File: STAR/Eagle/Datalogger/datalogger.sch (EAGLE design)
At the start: 9 parts, among them U1 MT25QL01GBBB8ESF-0AAT

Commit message: datalogger v. 2
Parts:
- removed C1: 100nF, resistor:C-USC0603
- removed CONNECTOR: J30J-31J30, CM_J30J:J30J-31J30
- removed R1: 4.7k, resistor:R-US_R0603
- removed U1: MT25QL01GBBB8ESF-0AAT, NR_IC:MT25QL01GBBB8ESF-0AAT
- added J1: J30J-25, CM_J30J:J30J-25
- added U$5: W25N01GV, NR_IC:W25N01GV
- R2: value (none) -> 1M
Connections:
- removed net N$1: R1.2, U1.!RESET!, U1.DQ3/!HOLD!
- removed net N$10: CONNECTOR.11
- removed net N$12: CONNECTOR.13
- removed net N$2: CONNECTOR.3
- removed net N$3: CONNECTOR.4
- removed net N$4: CONNECTOR.5
- removed net N$5: CONNECTOR.6
- removed net N$6: CONNECTOR.7
- removed net N$7: CONNECTOR.8
- removed net N$8: CONNECTOR.9
- removed net N$9: CONNECTOR.10
- removed net PB23: CONNECTOR.2, U1.!S!
- new net B: J1.18
- new net F: J1.9
- new net H: J1.19
- new net J: J1.6
- new net R: J1.14
- new net S: J1.7
- new net V: J1.8
- new net Y: J1.10
- net +3V3: now also J1.12, U$5.VCC; no longer C1.1, CONNECTOR.21, R1.1, U1.VCC
- net +5V: now also J1.15; no longer CONNECTOR.29
- net DATA1_N: now also J1.2; no longer CONNECTOR.22
- net DATA1_P: now also J1.4; no longer CONNECTOR.23
- net DATA2_N: now also J1.23; no longer CONNECTOR.25
- net DATA2_P: now also J1.22; no longer CONNECTOR.24
- net DATA3_N: now also J1.16; no longer CONNECTOR.30
- net DATA3_P: now also J1.17; no longer CONNECTOR.31
- net DATA4_N: now also J1.21; no longer CONNECTOR.16
- net DATA4_P: now also J1.20; no longer CONNECTOR.15
- net GND: now also J1.13, U$5.CS, U$5.GND, U$5.PAD; no longer C1.2, CONNECTOR.12, CONNECTOR.14, CONNECTOR.26, U1.VSS
- net MISO_FLASH: now also J1.1, U$5.MISO; no longer CONNECTOR.1, U1.DQ1
- net MISO_STAR: now also J1.25; no longer CONNECTOR.27
- net MOSI_FLASH: now also J1.3, U$5.MOSI; no longer CONNECTOR.18, U1.DQ0
- net MOSI_STAR: no longer CONNECTOR.19
- net SCK_FLASH: now also J1.5, U$5.CLK; no longer CONNECTOR.17, U1.C
- net SCK_STAR: now also J1.11; no longer CONNECTOR.20
- net SD_STAR: now also J1.24; no longer CONNECTOR.28

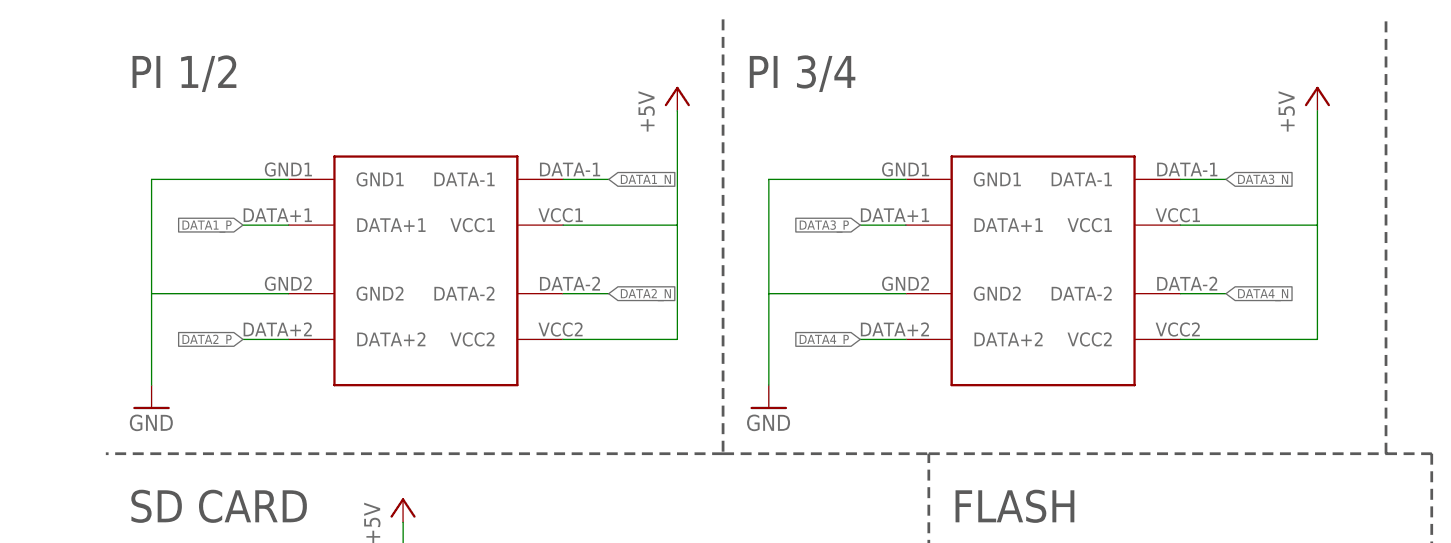
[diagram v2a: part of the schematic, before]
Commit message: fixed datalogger USB port
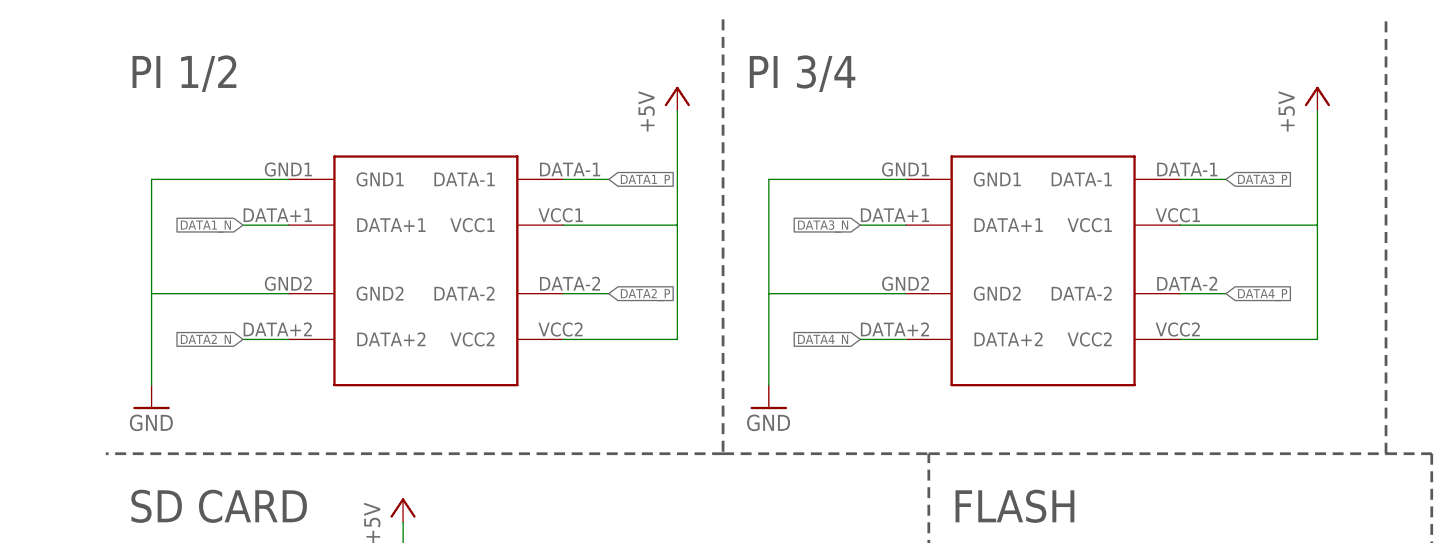
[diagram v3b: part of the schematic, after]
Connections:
- net DATA1_N: now also U$2.DATA+1; no longer U$2.DATA-1
- net DATA1_P: now also U$2.DATA-1; no longer U$2.DATA+1
- net DATA2_N: now also U$2.DATA+2; no longer U$2.DATA-2
- net DATA2_P: now also U$2.DATA-2; no longer U$2.DATA+2
- net DATA3_N: now also U$3.DATA+1; no longer U$3.DATA-1
- net DATA3_P: now also U$3.DATA-1; no longer U$3.DATA+1
- net DATA4_N: now also U$3.DATA+2; no longer U$3.DATA-2
- net DATA4_P: now also U$3.DATA-2; no longer U$3.DATA+2
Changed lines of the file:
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@@
 <net name="DATA1_P" class="0">
+<segment>
+<pinref part="J1" gate="G$1" pin="4"/>
+<wire x1="35.56" y1="106.68" x2="33.02" y2="106.68" width="0.1524" layer="91"/>
+<label x="33.02" y="106.68" size="1.016" layer="95" rot="R180" xref="yes"/>
+</segment>
+<segment>
+<pinref part="U$2" gate="G$1" pin="DATA-1"/>
+<wire x1="60.96" y1="254" x2="66.04" y2="254" width="0.1524" layer="91"/>
+<label x="66.04" y="254" size="1.016" layer="95" xref="yes"/>
+</segment>
+</net>
+<net name="DATA1_N" class="0">
+<segment>
+<pinref part="J1" gate="G$1" pin="2"/>
+<wire x1="35.56" y1="116.84" x2="33.02" y2="116.84" width="0.1524" layer="91"/>
+<label x="33.02" y="116.84" size="1.016" layer="95" rot="R180" xref="yes"/>
+</segment>
 <segment>
 <pinref part="U$2" gate="G$1" pin="DATA+1"/>
@@
 <label x="25.4" y="248.92" size="1.016" layer="95" rot="R180" xref="yes"/>
 </segment>
+</net>
+<net name="DATA2_P" class="0">
 <segment>
-<pinref part="J1" gate="G$1" pin="4"/>
-<wire x1="35.56" y1="106.68" x2="33.02" y2="106.68" width="0.1524" layer="91"/>
-<label x="33.02" y="106.68" size="1.016" layer="95" rot="R180" xref="yes"/>
+<pinref part="J1" gate="G$1" pin="22"/>
+<wire x1="45.72" y1="78.74" x2="48.26" y2="78.74" width="0.1524" layer="91"/>
+<label x="48.26" y="78.74" size="1.016" layer="95" xref="yes"/>
+</segment>
+<segment>
+<pinref part="U$2" gate="G$1" pin="DATA-2"/>
+<wire x1="60.96" y1="241.3" x2="66.04" y2="241.3" width="0.1524" layer="91"/>
+<label x="66.04" y="241.3" size="1.016" layer="95" xref="yes"/>
 </segment>
 </net>
-<net name="DATA1_N" class="0">
+<net name="DATA2_N" class="0">
 <segment>
-<pinref part="U$2" gate="G$1" pin="DATA-1"/>
-<wire x1="60.96" y1="254" x2="66.04" y2="254" width="0.1524" layer="91"/>
-<label x="66.04" y="254" size="1.016" layer="95" xref="yes"/>
+<pinref part="J1" gate="G$1" pin="23"/>
+<wire x1="45.72" y1="73.66" x2="48.26" y2="73.66" width="0.1524" layer="91"/>
+<label x="48.26" y="73.66" size="1.016" layer="95" xref="yes"/>
 </segment>
-<segment>
-<pinref part="J1" gate="G$1" pin="2"/>
-<wire x1="35.56" y1="116.84" x2="33.02" y2="116.84" width="0.1524" layer="91"/>
-<label x="33.02" y="116.84" size="1.016" layer="95" rot="R180" xref="yes"/>
-</segment>
-</net>
-<net name="DATA2_P" class="0">
 <segment>
 <pinref part="U$2" gate="G$1" pin="DATA+2"/>
@@
 <label x="25.4" y="236.22" size="1.016" layer="95" rot="R180" xref="yes"/>
 </segment>
+</net>
+<net name="DATA3_P" class="0">
 <segment>
-<pinref part="J1" gate="G$1" pin="22"/>
-<wire x1="45.72" y1="78.74" x2="48.26" y2="78.74" width="0.1524" layer="91"/>
-<label x="48.26" y="78.74" size="1.016" layer="95" xref="yes"/>
+<pinref part="J1" gate="G$1" pin="17"/>
+<wire x1="45.72" y1="104.14" x2="48.26" y2="104.14" width="0.1524" layer="91"/>
+<label x="48.26" y="104.14" size="1.016" layer="95" xref="yes"/>
+</segment>
+<segment>
+<pinref part="U$3" gate="G$1" pin="DATA-1"/>
+<wire x1="129.54" y1="254" x2="134.62" y2="254" width="0.1524" layer="91"/>
+<label x="134.62" y="254" size="1.016" layer="95" xref="yes"/>
 </segment>
 </net>
-<net name="DATA2_N" class="0">
+<net name="DATA3_N" class="0">
 <segment>
-<pinref part="U$2" gate="G$1" pin="DATA-2"/>
-<wire x1="60.96" y1="241.3" x2="66.04" y2="241.3" width="0.1524" layer="91"/>
-<label x="66.04" y="241.3" size="1.016" layer="95" xref="yes"/>
+<pinref part="J1" gate="G$1" pin="16"/>
+<wire x1="45.72" y1="109.22" x2="48.26" y2="109.22" width="0.1524" layer="91"/>
+<label x="48.26" y="109.22" size="1.016" layer="95" xref="yes"/>
 </segment>
-<segment>
-<pinref part="J1" gate="G$1" pin="23"/>
-<wire x1="45.72" y1="73.66" x2="48.26" y2="73.66" width="0.1524" layer="91"/>
-<label x="48.26" y="73.66" size="1.016" layer="95" xref="yes"/>
-</segment>
-</net>
-<net name="DATA3_P" class="0">
 <segment>
 <pinref part="U$3" gate="G$1" pin="DATA+1"/>
@@
 <label x="93.98" y="248.92" size="1.016" layer="95" rot="R180" xref="yes"/>
 </segment>
+</net>
+<net name="DATA4_P" class="0">
 <segment>
-<pinref part="J1" gate="G$1" pin="17"/>
-<wire x1="45.72" y1="104.14" x2="48.26" y2="104.14" width="0.1524" layer="91"/>
-<label x="48.26" y="104.14" size="1.016" layer="95" xref="yes"/>
+<pinref part="J1" gate="G$1" pin="20"/>
+<wire x1="45.72" y1="88.9" x2="48.26" y2="88.9" width="0.1524" layer="91"/>
+<label x="48.26" y="88.9" size="1.016" layer="95" xref="yes"/>
+</segment>
+<segment>
+<pinref part="U$3" gate="G$1" pin="DATA-2"/>
+<wire x1="129.54" y1="241.3" x2="134.62" y2="241.3" width="0.1524" layer="91"/>
+<label x="134.62" y="241.3" size="1.016" layer="95" xref="yes"/>
 </segment>
 </net>
-<net name="DATA3_N" class="0">
+<net name="DATA4_N" class="0">
 <segment>
-<pinref part="U$3" gate="G$1" pin="DATA-1"/>
-<wire x1="129.54" y1="254" x2="134.62" y2="254" width="0.1524" layer="91"/>
-<label x="134.62" y="254" size="1.016" layer="95" xref="yes"/>
+<pinref part="J1" gate="G$1" pin="21"/>
+<wire x1="45.72" y1="83.82" x2="48.26" y2="83.82" width="0.1524" layer="91"/>
+<label x="48.26" y="83.82" size="1.016" layer="95" xref="yes"/>
 </segment>
-<segment>
-<pinref part="J1" gate="G$1" pin="16"/>
-<wire x1="45.72" y1="109.22" x2="48.26" y2="109.22" width="0.1524" layer="91"/>
-<label x="48.26" y="109.22" size="1.016" layer="95" xref="yes"/>
-</segment>
-</net>
-<net name="DATA4_P" class="0">
 <segment>
 <pinref part="U$3" gate="G$1" pin="DATA+2"/>
@@
 <label x="93.98" y="236.22" size="1.016" layer="95" rot="R180" xref="yes"/>
 </segment>
-<segment>
-<pinref part="J1" gate="G$1" pin="20"/>
-<wire x1="45.72" y1="88.9" x2="48.26" y2="88.9" width="0.1524" layer="91"/>
-<label x="48.26" y="88.9" size="1.016" layer="95" xref="yes"/>
-</segment>
 </net>
-<net name="DATA4_N" class="0">
-<segment>
-<pinref part="U$3" gate="G$1" pin="DATA-2"/>
-<wire x1="129.54" y1="241.3" x2="134.62" y2="241.3" width="0.1524" layer="91"/>
-<label x="134.62" y="241.3" size="1.016" layer="95" xref="yes"/>
-</segment>
-<segment>
-<pinref part="J1" gate="G$1" pin="21"/>
-<wire x1="45.72" y1="83.82" x2="48.26" y2="83.82" width="0.1524" layer="91"/>
-<label x="48.26" y="83.82" size="1.016" layer="95" xref="yes"/>
-</segment>
-</net>
